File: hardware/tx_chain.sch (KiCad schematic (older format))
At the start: 34 parts, among them Q501 BCP56, Q502 IRL510, T501 TRANSFO2, U501 74LVC1G3157, U502 74LVC1G3157

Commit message: failsafe commit just before recreating netlist
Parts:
- added C? (x2): 1nF, symbol C
- added R? (x2): 100R, symbol R
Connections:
- net GND: now also C?.2, C?.2
- net TX_I: now also C?.1, R?.2; no longer U501.4 (A)
- net TX_Q: now also C?.1, R?.2; no longer U502.4 (A)
- new net: R?.1, U501.4 (A)
- new net: R?.1, U502.4 (A)
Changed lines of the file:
@@
 Comment4 ""
 $EndDescr
-Text HLabel 1750 3750 0    60   Input ~ 0
+Text HLabel 1400 3750 0    60   Input ~ 0
 TX_I
-Text HLabel 1750 4450 0    60   Input ~ 0
+Text HLabel 1400 4450 0    60   Input ~ 0
 TX_Q
 $Comp
@@
 	3100 4550 3100 4800
 Wire Wire Line
-	1750 4450 2250 4450
-Wire Wire Line
-	1750 3750 2250 3750
+	2000 4450 2250 4450
+Wire Wire Line
+	2000 3750 2250 3750
 Wire Wire Line
 	2150 3550 2150 3850
@@
 	0    -1   -1   0
 $EndComp
+$Comp
+L R R?
+U 1 1 57F1E4B0
+P 1850 3750
+F 0 "R?" V 1930 3750 50  0000 C CNN
+F 1 "100R" V 1850 3750 50  0000 C CNN
+F 2 "" V 1780 3750 50  0000 C CNN
+F 3 "" H 1850 3750 50  0000 C CNN
+	1    1850 3750
+	0    1    1    0
+$EndComp
+$Comp
+L R R?
+U 1 1 57F1E638
+P 1850 4450
+F 0 "R?" V 1930 4450 50  0000 C CNN
+F 1 "100R" V 1850 4450 50  0000 C CNN
+F 2 "" V 1780 4450 50  0000 C CNN
+F 3 "" H 1850 4450 50  0000 C CNN
+	1    1850 4450
+	0    1    1    0
+$EndComp
+Wire Wire Line
+	1700 4450 1400 4450
+Wire Wire Line
+	1700 3750 1400 3750
+$Comp
+L C C?
+U 1 1 57F1E8A9
+P 1400 4050
+F 0 "C?" H 1425 4150 50  0000 L CNN
+F 1 "1nF" H 1425 3950 50  0000 L CNN
+F 2 "" H 1438 3900 50  0000 C CNN
+F 3 "" H 1400 4050 50  0000 C CNN
+	1    1400 4050
+	-1   0    0    -1
+$EndComp
+$Comp
+L C C?
+U 1 1 57F1E9BB
+P 1400 4750
+F 0 "C?" H 1425 4850 50  0000 L CNN
+F 1 "1nF" H 1425 4650 50  0000 L CNN
+F 2 "" H 1438 4600 50  0000 C CNN
+F 3 "" H 1400 4750 50  0000 C CNN
+	1    1400 4750
+	-1   0    0    -1
+$EndComp
+$Comp
+L GND #PWR?
+U 1 1 57F1EA3D
+P 1400 4200
+F 0 "#PWR?" H 1400 3950 50  0001 C CNN
+F 1 "GND" H 1400 4050 50  0000 C CNN
+F 2 "" H 1400 4200 50  0000 C CNN
+F 3 "" H 1400 4200 50  0000 C CNN
+	1    1400 4200
+	1    0    0    -1
+$EndComp
+$Comp
+L GND #PWR?
+U 1 1 57F1EAC1
+P 1400 4900
+F 0 "#PWR?" H 1400 4650 50  0001 C CNN
+F 1 "GND" H 1400 4750 50  0000 C CNN
+F 2 "" H 1400 4900 50  0000 C CNN
+F 3 "" H 1400 4900 50  0000 C CNN
+	1    1400 4900
+	1    0    0    -1
+$EndComp
+Wire Wire Line
+	1400 4450 1400 4600
+Wire Wire Line
+	1400 3750 1400 3900
 $EndSCHEMATC

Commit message: 15% of layout done.. hopefully
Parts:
- C514, C515: renamed from C?; footprint (none) -> Capacitors_SMD:C_0805_HandSoldering
- R512, R513: renamed from R?; footprint (none) -> Resistors_SMD:R_0805_HandSoldering
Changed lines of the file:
@@
 $EndComp
 $Comp
-L R R?
+L R R512
 U 1 1 57F1E4B0
 P 1850 3750
-F 0 "R?" V 1930 3750 50  0000 C CNN
+F 0 "R512" V 1930 3750 50  0000 C CNN
 F 1 "100R" V 1850 3750 50  0000 C CNN
-F 2 "" V 1780 3750 50  0000 C CNN
+F 2 "Resistors_SMD:R_0805_HandSoldering" V 1780 3750 50  0001 C CNN
 F 3 "" H 1850 3750 50  0000 C CNN
 	1    1850 3750
@@
 $EndComp
 $Comp
-L R R?
+L R R513
 U 1 1 57F1E638
 P 1850 4450
-F 0 "R?" V 1930 4450 50  0000 C CNN
+F 0 "R513" V 1930 4450 50  0000 C CNN
 F 1 "100R" V 1850 4450 50  0000 C CNN
-F 2 "" V 1780 4450 50  0000 C CNN
+F 2 "Resistors_SMD:R_0805_HandSoldering" V 1780 4450 50  0001 C CNN
 F 3 "" H 1850 4450 50  0000 C CNN
 	1    1850 4450
@@
 	1700 3750 1400 3750
 $Comp
-L C C?
+L C C514
 U 1 1 57F1E8A9
 P 1400 4050
-F 0 "C?" H 1425 4150 50  0000 L CNN
+F 0 "C514" H 1425 4150 50  0000 L CNN
 F 1 "1nF" H 1425 3950 50  0000 L CNN
-F 2 "" H 1438 3900 50  0000 C CNN
+F 2 "Capacitors_SMD:C_0805_HandSoldering" H 1438 3900 50  0001 C CNN
 F 3 "" H 1400 4050 50  0000 C CNN
 	1    1400 4050
@@
 $EndComp
 $Comp
-L C C?
+L C C515
 U 1 1 57F1E9BB
 P 1400 4750
-F 0 "C?" H 1425 4850 50  0000 L CNN
+F 0 "C515" H 1425 4850 50  0000 L CNN
 F 1 "1nF" H 1425 4650 50  0000 L CNN
-F 2 "" H 1438 4600 50  0000 C CNN
+F 2 "Capacitors_SMD:C_0805_HandSoldering" H 1438 4600 50  0001 C CNN
 F 3 "" H 1400 4750 50  0000 C CNN
 	1    1400 4750
@@
 $EndComp
 $Comp
-L GND #PWR?
+L GND #PWR038
 U 1 1 57F1EA3D
 P 1400 4200
-F 0 "#PWR?" H 1400 3950 50  0001 C CNN
+F 0 "#PWR038" H 1400 3950 50  0001 C CNN
 F 1 "GND" H 1400 4050 50  0000 C CNN
 F 2 "" H 1400 4200 50  0000 C CNN
@@
 $EndComp
 $Comp
-L GND #PWR?
+L GND #PWR039
 U 1 1 57F1EAC1
 P 1400 4900
-F 0 "#PWR?" H 1400 4650 50  0001 C CNN
+F 0 "#PWR039" H 1400 4650 50  0001 C CNN
 F 1 "GND" H 1400 4750 50  0000 C CNN
 F 2 "" H 1400 4900 50  0000 C CNN

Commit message: halfway through layout
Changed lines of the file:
@@
 $EndComp
 $Comp
-L GND #PWR021
+L GND #PWR022
 U 1 1 57E4343C
 P 3100 4100
-F 0 "#PWR021" H 3100 3850 50  0001 C CNN
+F 0 "#PWR022" H 3100 3850 50  0001 C CNN
 F 1 "GND" H 3100 3950 50  0000 C CNN
 F 2 "" H 3100 4100 50  0000 C CNN
@@
 $EndComp
 $Comp
-L GND #PWR022
+L GND #PWR023
 U 1 1 57E4345E
 P 3100 4800
-F 0 "#PWR022" H 3100 4550 50  0001 C CNN
+F 0 "#PWR023" H 3100 4550 50  0001 C CNN
 F 1 "GND" H 3100 4650 50  0000 C CNN
 F 2 "" H 3100 4800 50  0000 C CNN
@@
 $EndComp
 $Comp
-L +Vlogic #PWR023
+L +Vlogic #PWR024
 U 1 1 57E434AC
 P 2150 3550
-F 0 "#PWR023" H 2150 3350 50  0001 C CNN
+F 0 "#PWR024" H 2150 3350 50  0001 C CNN
 F 1 "+Vlogic" H 2150 3750 50  0000 C CNN
 F 2 "" H 2150 3550 50  0000 C CNN
@@
 $EndComp
 $Comp
-L +Vlogic #PWR024
+L +Vlogic #PWR025
 U 1 1 57E434C4
 P 2150 4250
-F 0 "#PWR024" H 2150 4050 50  0001 C CNN
+F 0 "#PWR025" H 2150 4050 50  0001 C CNN
 F 1 "+Vlogic" H 2150 4450 50  0000 C CNN
 F 2 "" H 2150 4250 50  0000 C CNN
@@
 $EndComp
 $Comp
-L GND #PWR025
+L GND #PWR026
 U 1 1 57E43B57
 P 3650 4450
-F 0 "#PWR025" H 3650 4200 50  0001 C CNN
+F 0 "#PWR026" H 3650 4200 50  0001 C CNN
 F 1 "GND" H 3650 4300 50  0000 C CNN
 F 2 "" H 3650 4450 50  0000 C CNN
@@
 $EndComp
 $Comp
-L GND #PWR026
+L GND #PWR027
 U 1 1 57E43B98
 P 5100 4800
-F 0 "#PWR026" H 5100 4550 50  0001 C CNN
+F 0 "#PWR027" H 5100 4550 50  0001 C CNN
 F 1 "GND" H 5100 4650 50  0000 C CNN
 F 2 "" H 5100 4800 50  0000 C CNN
@@
 $EndComp
 $Comp
-L GND #PWR027
+L GND #PWR028
 U 1 1 57E44284
 P 6600 4800
-F 0 "#PWR027" H 6600 4550 50  0001 C CNN
+F 0 "#PWR028" H 6600 4550 50  0001 C CNN
 F 1 "GND" H 6600 4650 50  0000 C CNN
 F 2 "" H 6600 4800 50  0000 C CNN
@@
 $EndComp
 $Comp
-L GND #PWR028
+L GND #PWR029
 U 1 1 57E451F7
 P 6850 3550
-F 0 "#PWR028" H 6850 3300 50  0001 C CNN
+F 0 "#PWR029" H 6850 3300 50  0001 C CNN
 F 1 "GND" H 6850 3400 50  0000 C CNN
 F 2 "" H 6850 3550 50  0000 C CNN
@@
 $EndComp
 $Comp
-L GND #PWR029
+L GND #PWR030
 U 1 1 57E458EE
 P 8000 3150
-F 0 "#PWR029" H 8000 2900 50  0001 C CNN
+F 0 "#PWR030" H 8000 2900 50  0001 C CNN
 F 1 "GND" H 8000 3000 50  0000 C CNN
 F 2 "" H 8000 3150 50  0000 C CNN
@@
 $EndComp
 $Comp
-L Vin #Vin030
+L Vin #Vin031
 U 1 1 57E45ADD
 P 8350 2100
-F 0 "#Vin030" H 8500 2150 60  0001 C CNN
+F 0 "#Vin031" H 8500 2150 60  0001 C CNN
 F 1 "Vin" H 8200 2150 60  0000 C CNN
 F 2 "" H 8350 2100 60  0001 C CNN
@@
 $EndComp
 $Comp
-L GND #PWR031
+L GND #PWR032
 U 1 1 57E45E2D
 P 8350 4900
-F 0 "#PWR031" H 8350 4650 50  0001 C CNN
+F 0 "#PWR032" H 8350 4650 50  0001 C CNN
 F 1 "GND" H 8350 4750 50  0000 C CNN
 F 2 "" H 8350 4900 50  0000 C CNN
@@
 $EndComp
 $Comp
-L GND #PWR032
+L GND #PWR033
 U 1 1 57E465CB
 P 9500 4100
-F 0 "#PWR032" H 9500 3850 50  0001 C CNN
+F 0 "#PWR033" H 9500 3850 50  0001 C CNN
 F 1 "GND" H 9500 3950 50  0000 C CNN
 F 2 "" H 9500 4100 50  0000 C CNN
@@
 $EndComp
 $Comp
-L GND #PWR033
+L GND #PWR034
 U 1 1 57E471D5
 P 5700 3800
-F 0 "#PWR033" H 5700 3550 50  0001 C CNN
+F 0 "#PWR034" H 5700 3550 50  0001 C CNN
 F 1 "GND" H 5700 3650 50  0000 C CNN
 F 2 "" H 5700 3800 50  0000 C CNN
@@
 $EndComp
 $Comp
-L GND #PWR034
+L GND #PWR035
 U 1 1 57EBA5D8
 P 7950 5550
-F 0 "#PWR034" H 7950 5300 50  0001 C CNN
+F 0 "#PWR035" H 7950 5300 50  0001 C CNN
 F 1 "GND" H 7950 5400 50  0000 C CNN
 F 2 "" H 7950 5550 50  0000 C CNN
@@
 $EndComp
 $Comp
-L GND #PWR035
+L GND #PWR036
 U 1 1 57EBA6B5
 P 8550 5600
-F 0 "#PWR035" H 8550 5350 50  0001 C CNN
+F 0 "#PWR036" H 8550 5350 50  0001 C CNN
 F 1 "GND" H 8550 5450 50  0000 C CNN
 F 2 "" H 8550 5600 50  0000 C CNN
@@
 $EndComp
 $Comp
-L GND #PWR036
+L GND #PWR037
 U 1 1 57EAC40D
 P 9100 5600
-F 0 "#PWR036" H 9100 5350 50  0001 C CNN
+F 0 "#PWR037" H 9100 5350 50  0001 C CNN
 F 1 "GND" H 9100 5450 50  0000 C CNN
 F 2 "" H 9100 5600 50  0000 C CNN
@@
 Wire Wire Line
 	9100 5600 9100 5550
-$Comp
-L PWR_FLAG #FLG037
-U 1 1 57EE999B
-P 8750 2100
-F 0 "#FLG037" H 8750 2195 50  0001 C CNN
-F 1 "PWR_FLAG" H 8750 2280 50  0000 C CNN
-F 2 "" H 8750 2100 50  0000 C CNN
-F 3 "" H 8750 2100 50  0000 C CNN
-	1    8750 2100
-	1    0    0    -1
-$EndComp
 Wire Wire Line
 	8750 2100 8350 2100
@@
 Wire Wire Line
 	1400 3750 1400 3900
+Connection ~ 8350 2100
 $EndSCHEMATC

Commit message: All components are placed. GND and +Vlogic copper fills still undone
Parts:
- D501: symbol LED -> LED-RESCUE-dodekaedri
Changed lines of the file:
@@
 Connection ~ 8000 2800
 $Comp
-L LED D501
+L LED-RESCUE-dodekaedri D501
 U 1 1 57F06BC9
 P 5700 3600

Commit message: Changed some component values
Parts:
- R503: value 50R -> 100R
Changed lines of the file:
@@
 P 6600 3350
 F 0 "R503" V 6680 3350 50  0000 C CNN
-F 1 "50R" V 6600 3350 50  0000 C CNN
+F 1 "100R" V 6600 3350 50  0000 C CNN
 F 2 "Resistors_SMD:R_0805_HandSoldering" V 6530 3350 50  0001 C CNN
 F 3 "" H 6600 3350 50  0000 C CNN

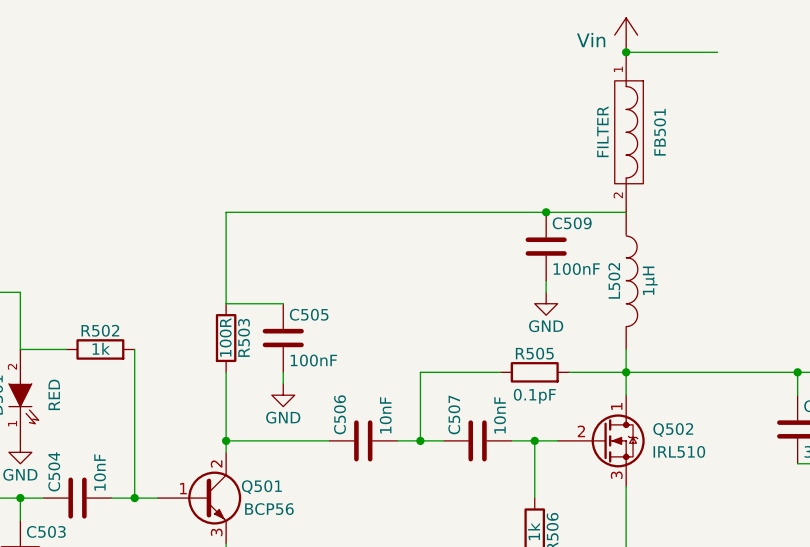
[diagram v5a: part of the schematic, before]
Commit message: Changed TX driver supply voltage to 3.3V
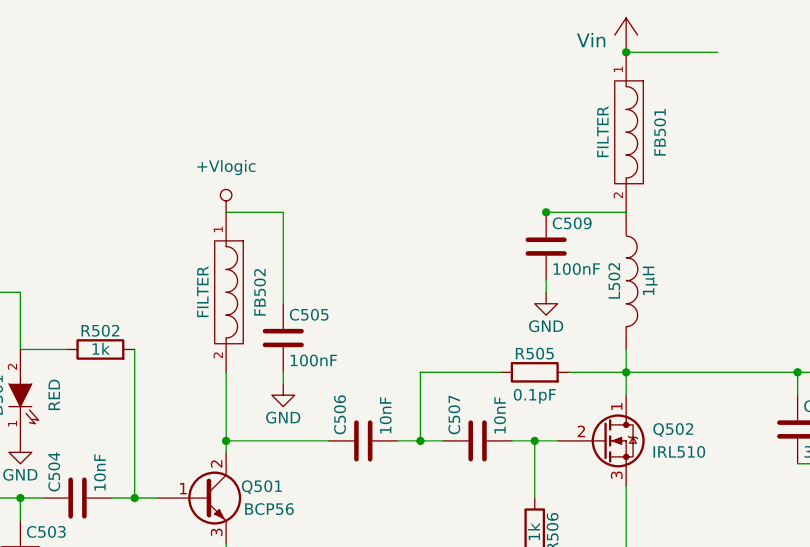
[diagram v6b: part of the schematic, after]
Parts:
- removed R503: 100R, Resistors_SMD:R_0805_HandSoldering, symbol R
- added FB502: FILTER, Resistors_SMD:R_0805_HandSoldering, symbol FILTER
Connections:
- net +Vlogic: now also C505.1, FB502.1
- net at C506.1, Q501.2 (C): now also FB502.2
- net at C509.1, FB501.2, L502.1: no longer C505.1
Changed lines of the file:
@@
-$EndComp
-$Comp
-L R R503
-U 1 1 57E45175
-P 6600 3350
-F 0 "R503" V 6680 3350 50  0000 C CNN
-F 1 "100R" V 6600 3350 50  0000 C CNN
-F 2 "Resistors_SMD:R_0805_HandSoldering" V 6530 3350 50  0001 C CNN
-F 3 "" H 6600 3350 50  0000 C CNN
-	1    6600 3350
-	1    0    0    -1
 $EndComp
 $Comp
@@
 	6600 4350 6600 4250
 Wire Wire Line
-	6600 2800 6600 3200
-Wire Wire Line
-	6600 3200 6850 3200
-Wire Wire Line
 	6850 3500 6850 3550
 Wire Wire Line
@@
 Wire Wire Line
 	8000 3100 8000 3150
-Wire Wire Line
-	6600 2800 8350 2800
 Connection ~ 8350 3500
 Wire Wire Line
@@
 	1400 3750 1400 3900
 Connection ~ 8350 2100
+Wire Wire Line
+	8000 2800 8350 2800
+$Comp
+L +Vlogic #PWR040
+U 1 1 5881380E
+P 6600 2800
+F 0 "#PWR040" H 6600 2600 50  0001 C CNN
+F 1 "+Vlogic" H 6600 3000 50  0000 C CNN
+F 2 "" H 6600 2800 50  0000 C CNN
+F 3 "" H 6600 2800 50  0000 C CNN
+	1    6600 2800
+	1    0    0    -1
+$EndComp
+$Comp
+L FILTER FB502
+U 1 1 5881386E
+P 6600 3150
+F 0 "FB502" H 6600 3300 50  0000 C CNN
+F 1 "FILTER" H 6600 3050 50  0000 C CNN
+F 2 "Resistors_SMD:R_0805_HandSoldering" H 6600 3150 50  0001 C CNN
+F 3 "" H 6600 3150 50  0000 C CNN
+	1    6600 3150
+	0    1    1    0
+$EndComp
+Wire Wire Line
+	6850 3200 6850 2800
+Wire Wire Line
+	6850 2800 6600 2800
 $EndSCHEMATC
